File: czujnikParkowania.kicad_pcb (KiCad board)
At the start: 2 copper layers, 46 parts, among them J1 Screw_Terminal_01x03, Q1 BC817, Q2 IRF7404, Q3 BC817, Q4 BC817, Q5 BC817, SW1 SW_Push, U1 DC56-11SEKWA, U2 LM7805_TO220, U3 HC-SR04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

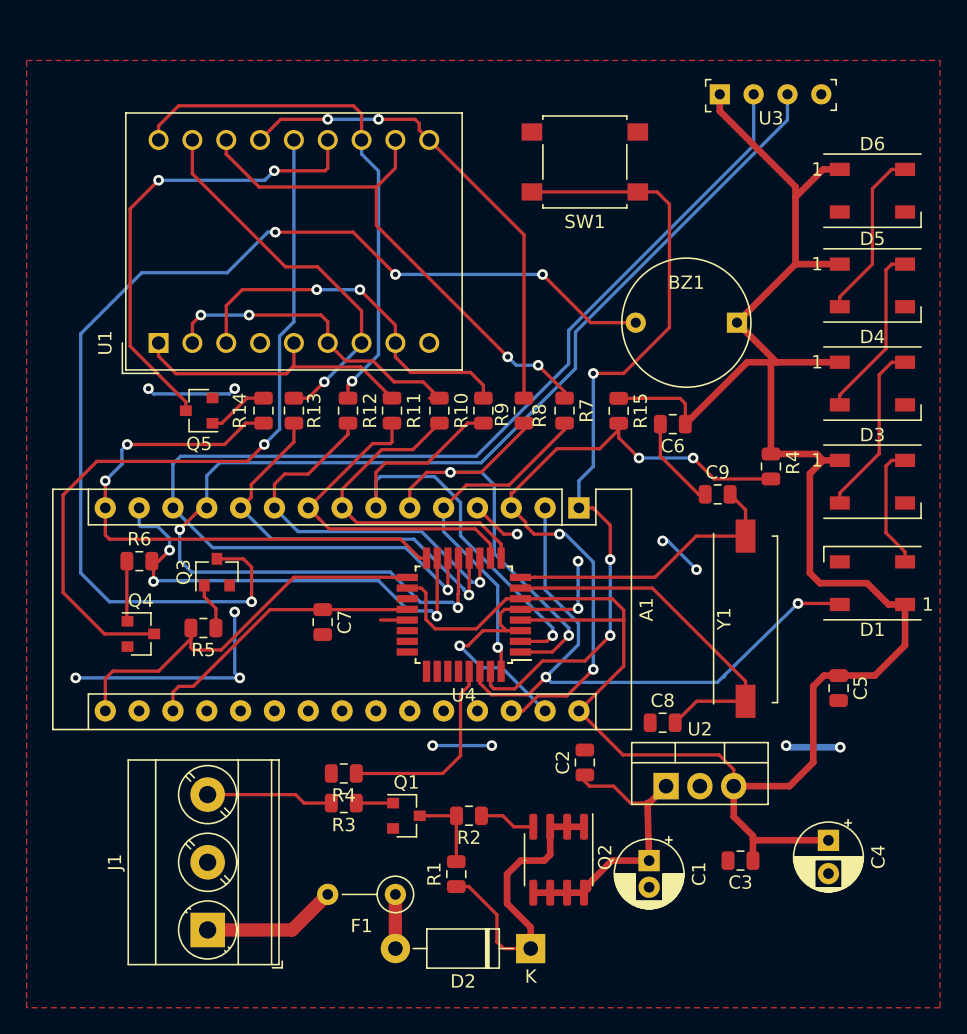
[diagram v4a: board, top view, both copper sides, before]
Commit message: added ground zones through vias
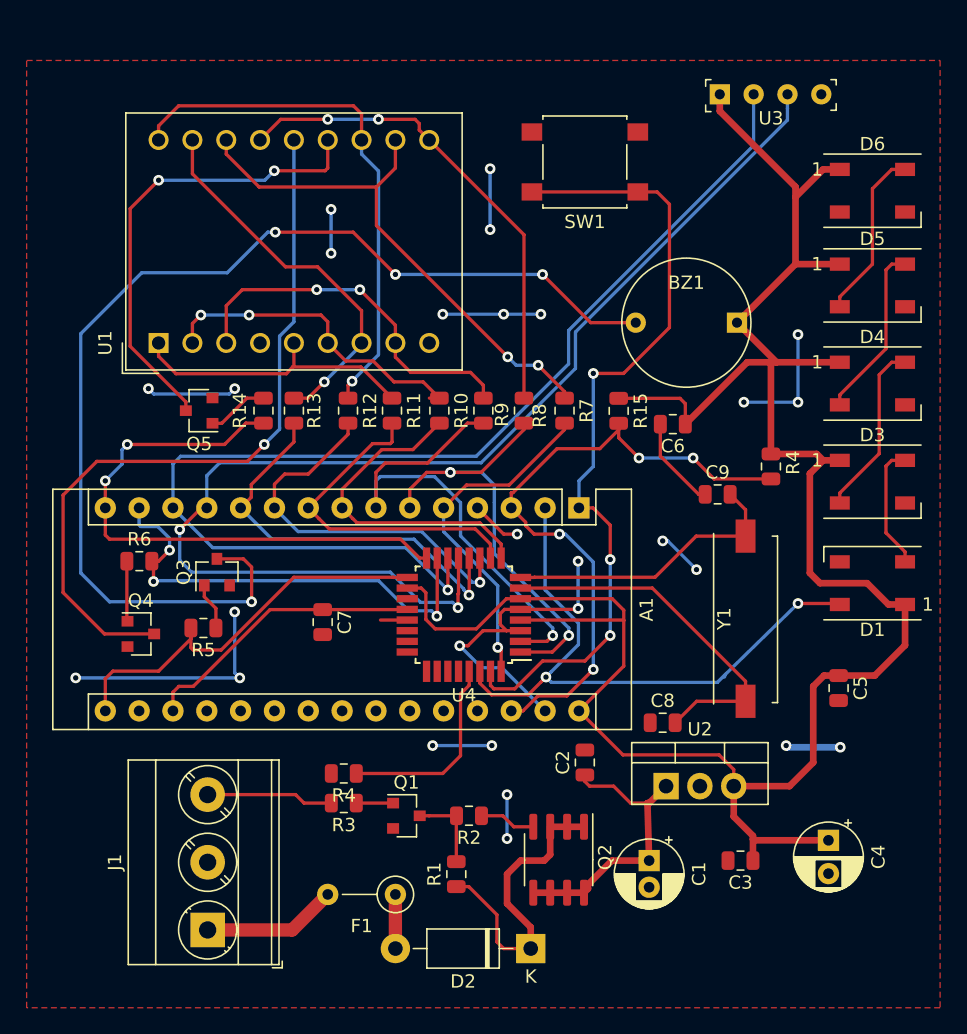
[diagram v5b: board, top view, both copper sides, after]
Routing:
- net GND: track 73.5 -> 101.2 mm, vias 15 -> 27
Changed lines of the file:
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@@
     (thickness 1.6)
     (drawings 0)
-    (tracks 567)
+    (tracks 586)
     (zones 0)
     (modules 46)
@@
     (visible_elements 7FFFFFFF)
     (pcbplotparams
-      (layerselection 0x010fc_ffffffff)
+      (layerselection 0x030fc_ffffffff)
       (usegerberextensions false)
       (usegerberattributes false)
@@
     )
   )
+  (via (at 51.308 76.2) (size 0.8) (drill 0.4) (layers F.Cu B.Cu) (net 4))
+  (via (at 38.1 28.956) (size 0.8) (drill 0.4) (layers F.Cu B.Cu) (net 4))
+  (via (at 73.152 38.354) (size 0.8) (drill 0.4) (layers F.Cu B.Cu) (net 4))
+  (via (at 46.482 36.83) (size 0.8) (drill 0.4) (layers F.Cu B.Cu) (net 4))
+  (via (at 53.848 36.83) (size 0.8) (drill 0.4) (layers F.Cu B.Cu) (net 4))
+  (via (at 50.038 30.48) (size 0.8) (drill 0.4) (layers F.Cu B.Cu) (net 4))
+  (via (at 73.152 43.434) (size 0.8) (drill 0.4) (layers F.Cu B.Cu) (net 4))
   (via (at 73.152 58.547) (size 0.8) (drill 0.4) (layers F.Cu B.Cu) (net 1))
   (segment (start 76.29 58.623) (end 76.276 58.623) (width 0.25) (layer F.Cu) (net 1))
@@
   (via (at 50.165 69.215) (size 0.8) (drill 0.4) (layers F.Cu B.Cu) (net 4))
   (segment (start 45.72 69.215) (end 50.165 69.215) (width 0.25) (layer B.Cu) (net 4))
+  (via (at 69.088 43.434) (size 0.8) (drill 0.4) (layers F.Cu B.Cu) (net 4))
+  (segment (start 69.088 43.434) (end 73.152 43.434) (width 0.25) (layer B.Cu) (net 4))
+  (via (at 50.038 25.908) (size 0.8) (drill 0.4) (layers F.Cu B.Cu) (net 4))
+  (segment (start 50.038 25.908) (end 50.038 30.48) (width 0.25) (layer B.Cu) (net 4))
+  (via (at 51.054 36.83) (size 0.8) (drill 0.4) (layers F.Cu B.Cu) (net 4))
+  (segment (start 51.054 36.83) (end 53.848 36.83) (width 0.25) (layer B.Cu) (net 4))
+  (segment (start 51.054 36.83) (end 46.482 36.83) (width 0.25) (layer B.Cu) (net 4))
+  (via (at 38.1 32.258) (size 0.8) (drill 0.4) (layers F.Cu B.Cu) (net 4))
+  (segment (start 73.152 38.354) (end 73.152 43.434) (width 0.25) (layer B.Cu) (net 4))
+  (segment (start 38.1 28.956) (end 38.1 32.258) (width 0.25) (layer B.Cu) (net 4))
+  (via (at 51.308 72.898) (size 0.8) (drill 0.4) (layers F.Cu B.Cu) (net 4))
+  (segment (start 51.308 72.898) (end 51.308 76.2) (width 0.25) (layer B.Cu) (net 4))
   (segment (start 55.626 45.0065) (end 55.626 45.494) (width 0.25) (layer F.Cu) (net 5))
   (via (at 50.6095 61.849) (size 0.8) (drill 0.4) (layers F.Cu B.Cu) (net 5))
@@
     (polygon
       (pts
-        (xy 83.82 88.9) (xy 15.24 88.9) (xy 15.24 15.24) (xy 83.82 15.24)
+        (xy 83.82 88.9) (xy 15.24 88.9) (xy 15.24 17.78) (xy 83.82 17.78)
       )
     )
